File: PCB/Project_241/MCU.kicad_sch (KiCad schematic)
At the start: 24 parts, among them J1 BOOT MODE, J3 USB_B_Micro, J4 SPI CONNECTOR, SW1 RESET, U1 STM32F103C8T6, U2 USBLC6-2SC6

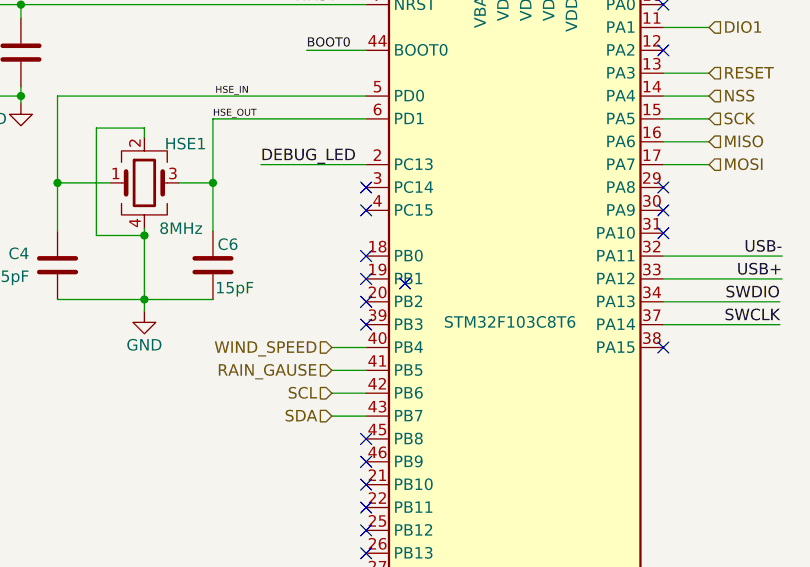
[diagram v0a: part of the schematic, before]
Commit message: update schematic
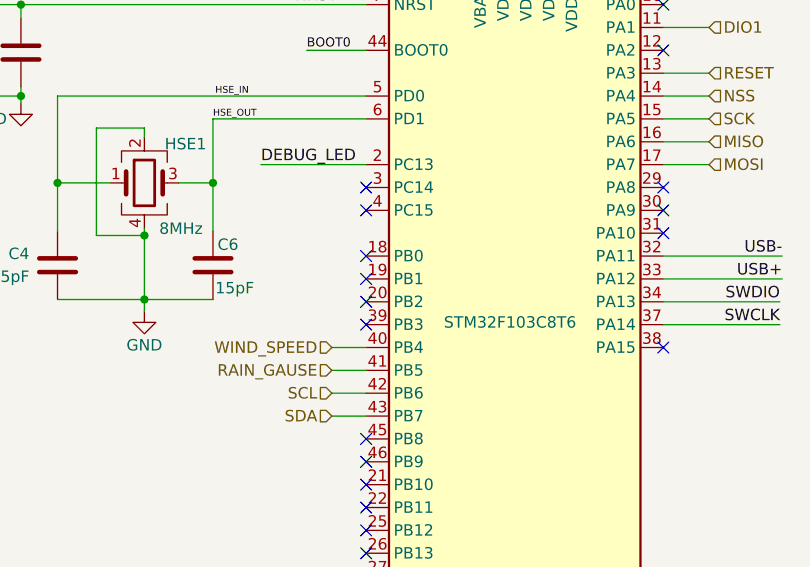
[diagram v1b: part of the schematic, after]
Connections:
- no-connect marks 22 -> 21
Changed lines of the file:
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@@
-	)
-	(no_connect
-		(at 129.286 107.442)
 	)
 	(no_connect

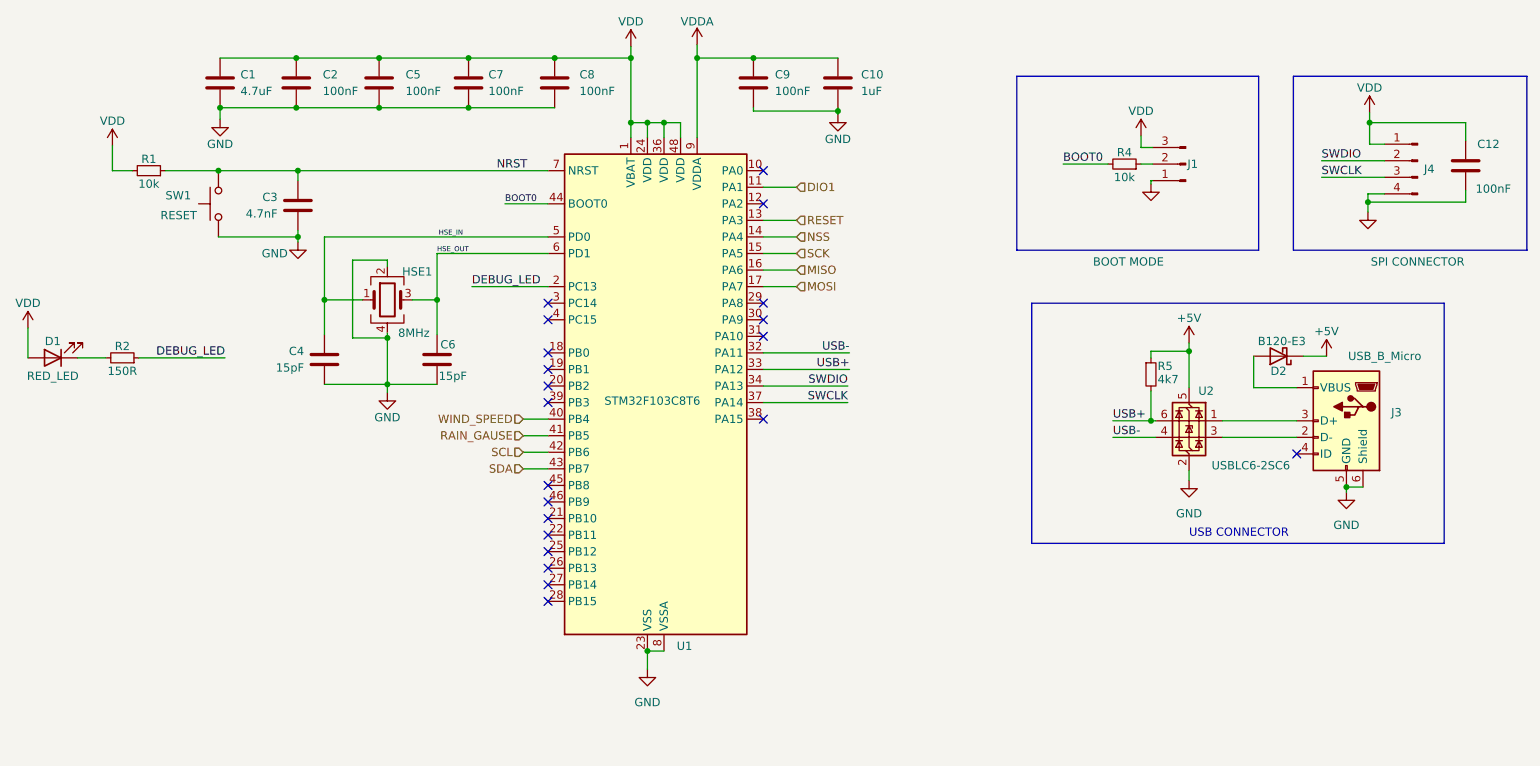
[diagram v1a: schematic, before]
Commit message: update schematic
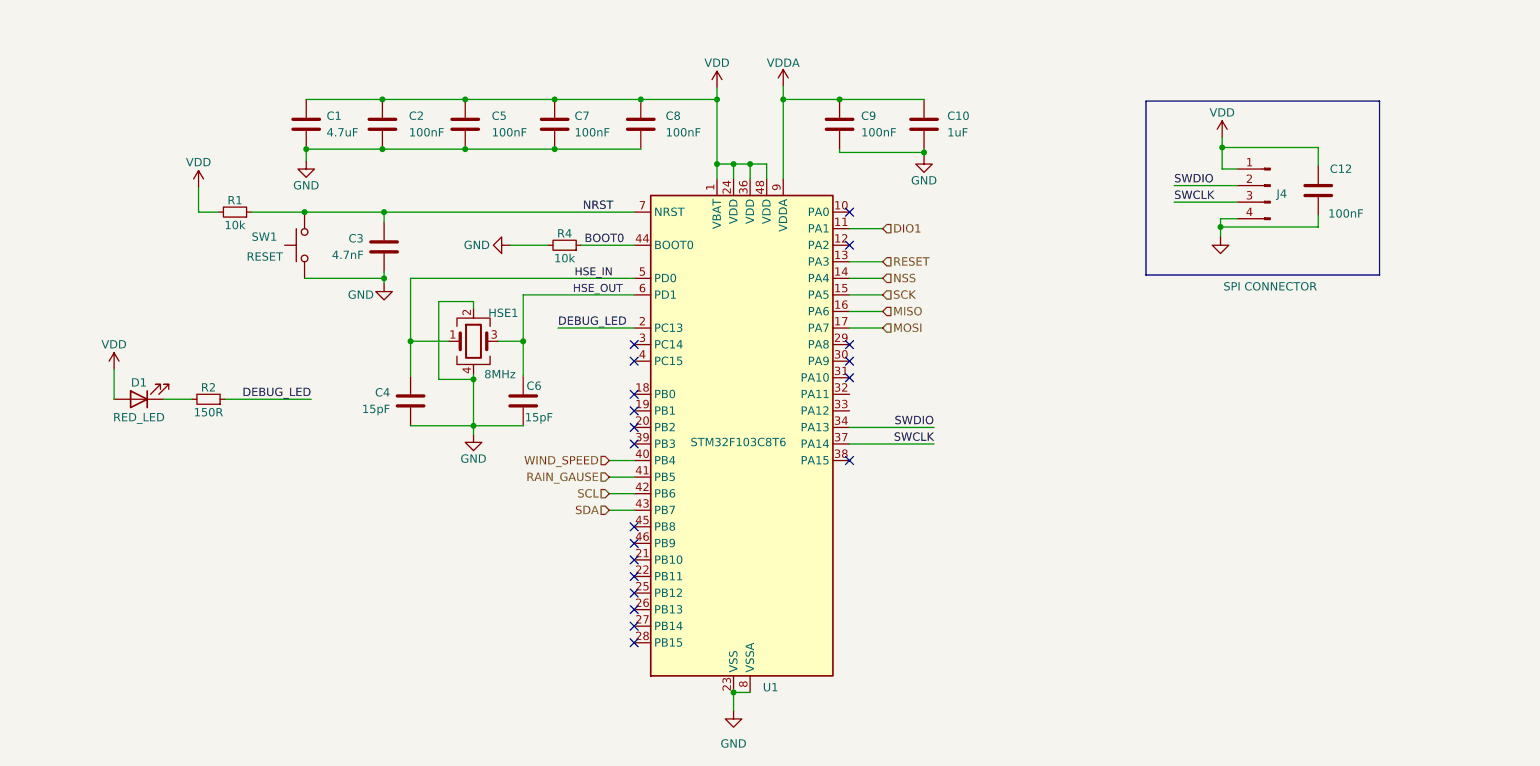
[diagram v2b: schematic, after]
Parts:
- removed D2: B120-E3, Diode_SMD:D_SOD-123, symbol Diode:B120-E3
- removed J1: BOOT MODE, Connector_PinHeader_2.54mm:PinHeader_1x03_P2.54mm_Vertical, symbol Connector:Conn_01x03_Pin
- removed J3: USB_B_Micro, Connector_USB:USB_Micro-B_Molex_47346-0001, symbol Connector:USB_B_Micro
- removed R5: 4k7, Resistor_SMD:R_0603_1608Metric, symbol Device:R_Small
- removed U2: USBLC6-2SC6, Package_TO_SOT_SMD:SOT-23-6, symbol Power_Protection:USBLC6-2SC6
- C1, C10, C12, C2, C3, C4, C5, C6, C7, C8, C9: footprint Capacitor_SMD:C_0402_1005Metric -> Capacitor_SMD:C_0603_1608Metric
- D1: footprint LED_SMD:LED_0805_2012Metric -> LED_SMD:LED_0603_1608Metric
- J4: footprint Connector_PinHeader_2.54mm:PinHeader_1x04_P2.54mm_Vertical -> IVSFootprint:XH_4P_2.54mm_Horizontal
- SW1: footprint Button_SMD:Button_3x6_SMD -> Button_Switch_SMD:SW_SPST_PTS647_Sx38
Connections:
- net BOOT0: now also R4.1; no longer R4.2
- net GND: now also R4.2
- net USB+: no longer names the net of U1.33 (PA12)
- net USB-: no longer names the net of U1.32 (PA11)
- no-connect marks 21 -> 20
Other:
- note removed: "USB CONNECTOR"
- moved on the sheet: C1, C10, C12, C2, C3, C4, C5, C6, C7, C8, C9, D1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

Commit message: update gerber
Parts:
- added D4: GREEN_LED, LED_SMD:LED_0603_1608Metric, symbol Device:LED
- added J1: UART_CONNECTOR, Connector_PinHeader_2.54mm:PinHeader_1x03_P2.54mm_Vertical, symbol Connector:Conn_01x03_Pin
- added R11: 56R, Resistor_SMD:R_0603_1608Metric, symbol Device:R_Small
- J4: footprint IVSFootprint:XH_4P_2.54mm_Horizontal -> Connector_PinHeader_2.54mm:PinHeader_1x04_P2.54mm_Vertical
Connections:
- net RESET is gone; now on net DIO1: U1.13 (PA3)
- net DIO1: no longer U1.11 (PA1)
- net GND: now also J1.3 (Pin_3)
- net VDD: now also D4.2 (A)
- net LORA_RESET: now reaches U1.12 (PA2)
- net DEBUG_TX: now reaches U1.21 (PB10)
- net DEBUG_TX: now also J1.1 (Pin_1)
- net DEBUG_RX: now reaches U1.22 (PB11)
- net DEBUG_RX: now also J1.2 (Pin_2)
- net LED_PC14: now reaches U1.3 (PC14)
- net LED_PC14: now also R11.1
- net GPS_TX: now reaches U1.30 (PA9)
- net GPS_RX: now reaches U1.31 (PA10)
- new net: D4.1 (K), R11.2
- no-connect marks 20 -> 17
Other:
- moved on the sheet: C12, C4, C6, HSE1, J4
